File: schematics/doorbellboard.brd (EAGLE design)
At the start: 25.4 x 68.6 mm, 7 parts

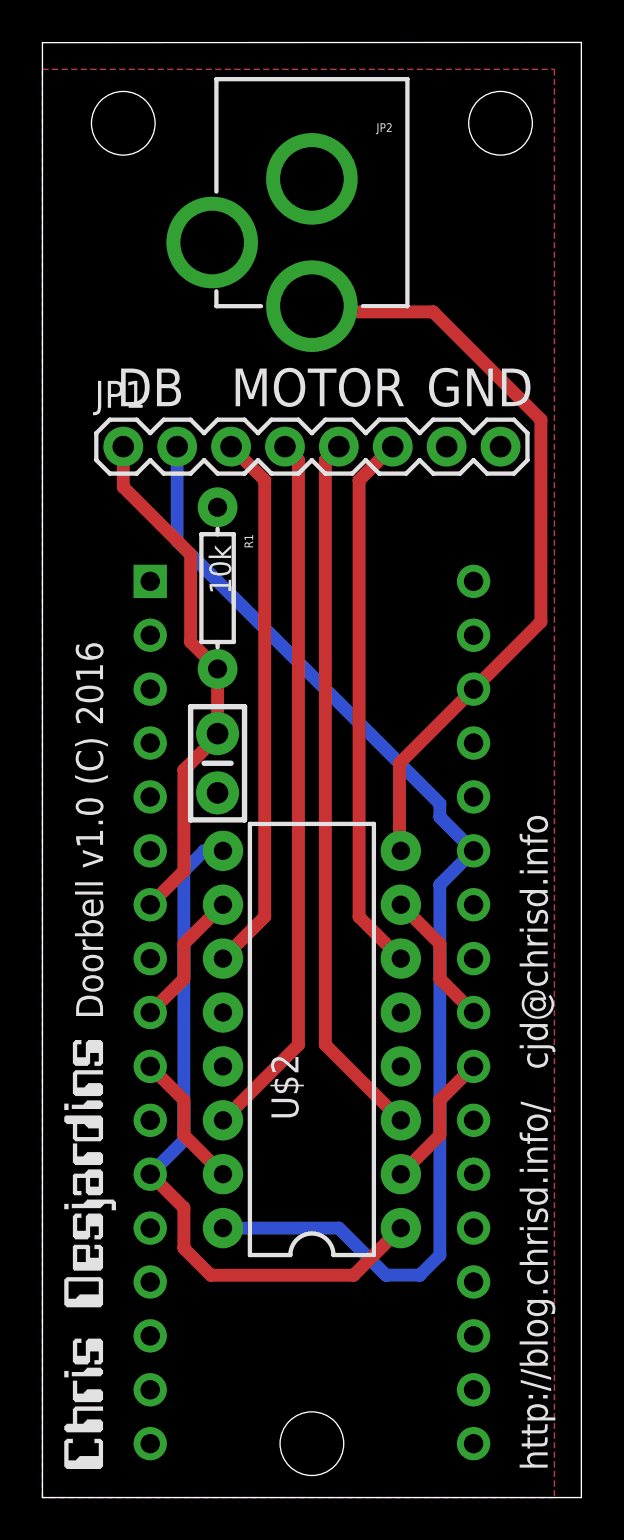
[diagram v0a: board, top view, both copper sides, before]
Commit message: Add OSHW logo
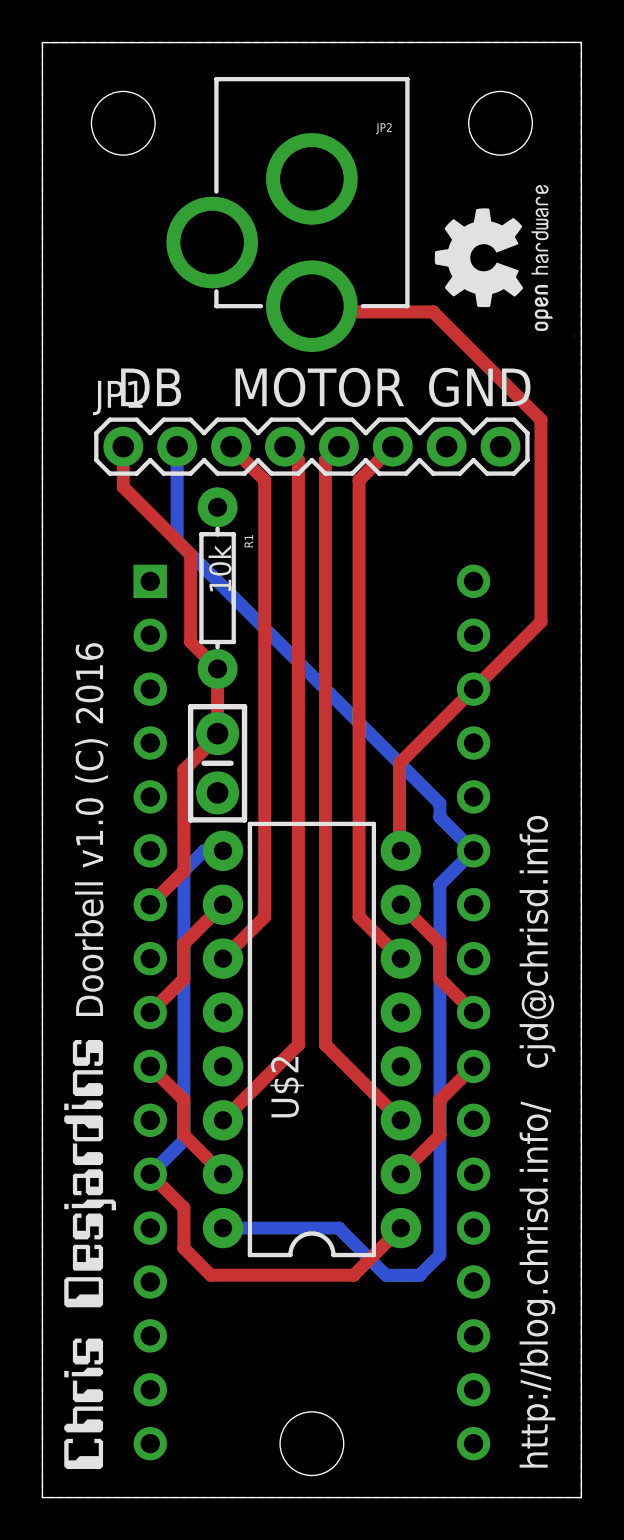
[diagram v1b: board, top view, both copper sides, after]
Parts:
- added U$4: (no value), bfl:OSHW2
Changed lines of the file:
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@@
 </element>
 <element name="U$3" library="desjardins" package="LOGO" value="" x="2.8575" y="1.27" rot="R90"/>
+<element name="U$4" library="bfl" package="OSHW2" value="" x="25.0825" y="54.61" rot="R90"/>
 </elements>
 <signals>
@@
 <polygon width="0.4064" layer="16">
 <vertex x="0" y="0"/>
-<vertex x="0" y="67.31"/>
-<vertex x="24.13" y="67.31"/>
-<vertex x="24.13" y="0"/>
+<vertex x="0" y="68.58"/>
+<vertex x="25.4" y="68.58"/>
+<vertex x="25.4" y="0"/>
 </polygon>
 <polygon width="0.4064" layer="1">
 <vertex x="0" y="0"/>
-<vertex x="0" y="67.31"/>
-<vertex x="24.13" y="67.31"/>
-<vertex x="24.13" y="0"/>
+<vertex x="0" y="68.58"/>
+<vertex x="25.4" y="68.58"/>
+<vertex x="25.4" y="0"/>
 </polygon>
 </signal>

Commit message: Rotate board
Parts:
- moved JP2 80.8 mm to (69.8, 12.7), turned to 90 degrees
- moved U$4 61.8 mm to (54.6, 0.32), turned to 0 degrees
- moved JP1 53.6 mm to (49.5, 21.6), turned to 270 degrees
- moved R1 43.1 mm to (42.9, 17.1), turned to 180 degrees
- moved C1 31.6 mm to (34.6, 17.1), turned to 0 degrees
- moved U$1 23.4 mm to (-1.27, 21.6), turned to 270 degrees
- moved U$3 21.3 mm to (1.27, 22.5), turned to 0 degrees
- moved U$2 12.6 mm to (21.6, 12.7), turned to 0 degrees
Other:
- board size 25.4 x 68.6 mm -> 68.6 x 25.4 mm

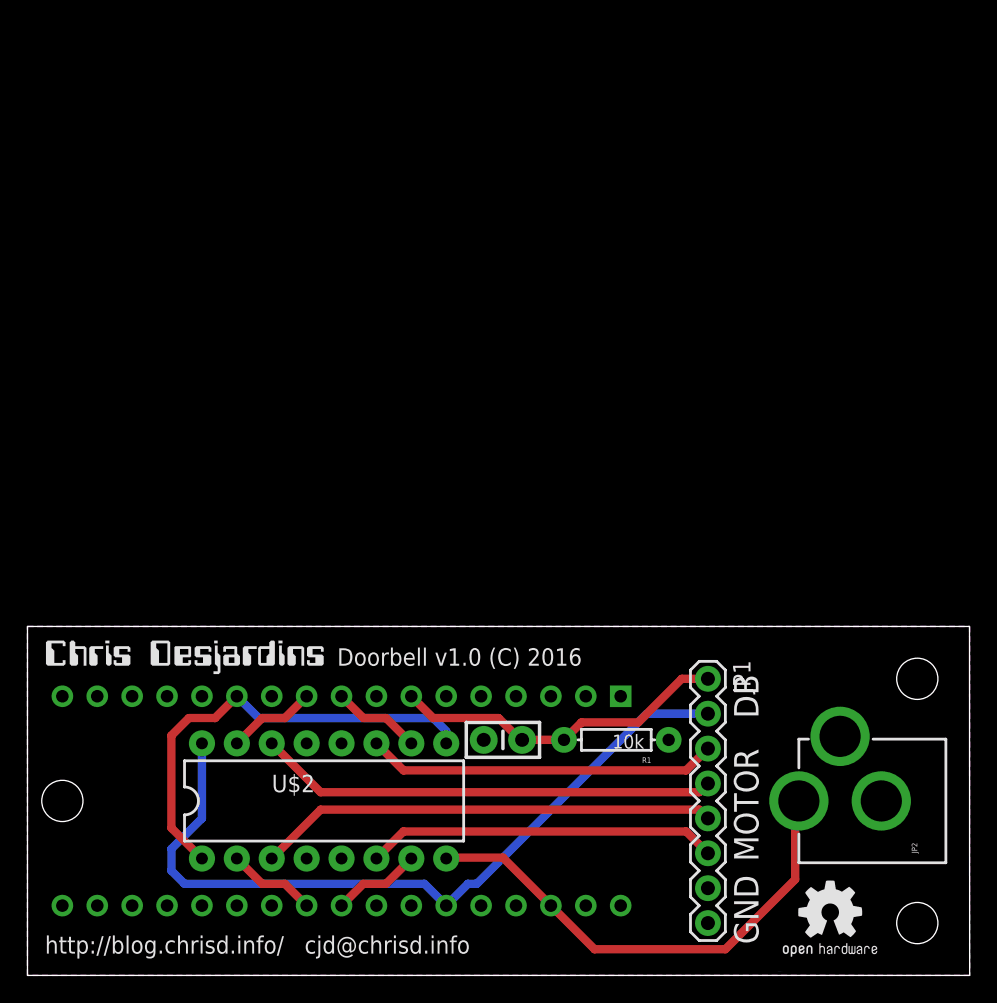
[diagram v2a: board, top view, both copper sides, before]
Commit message: Add some LEDs
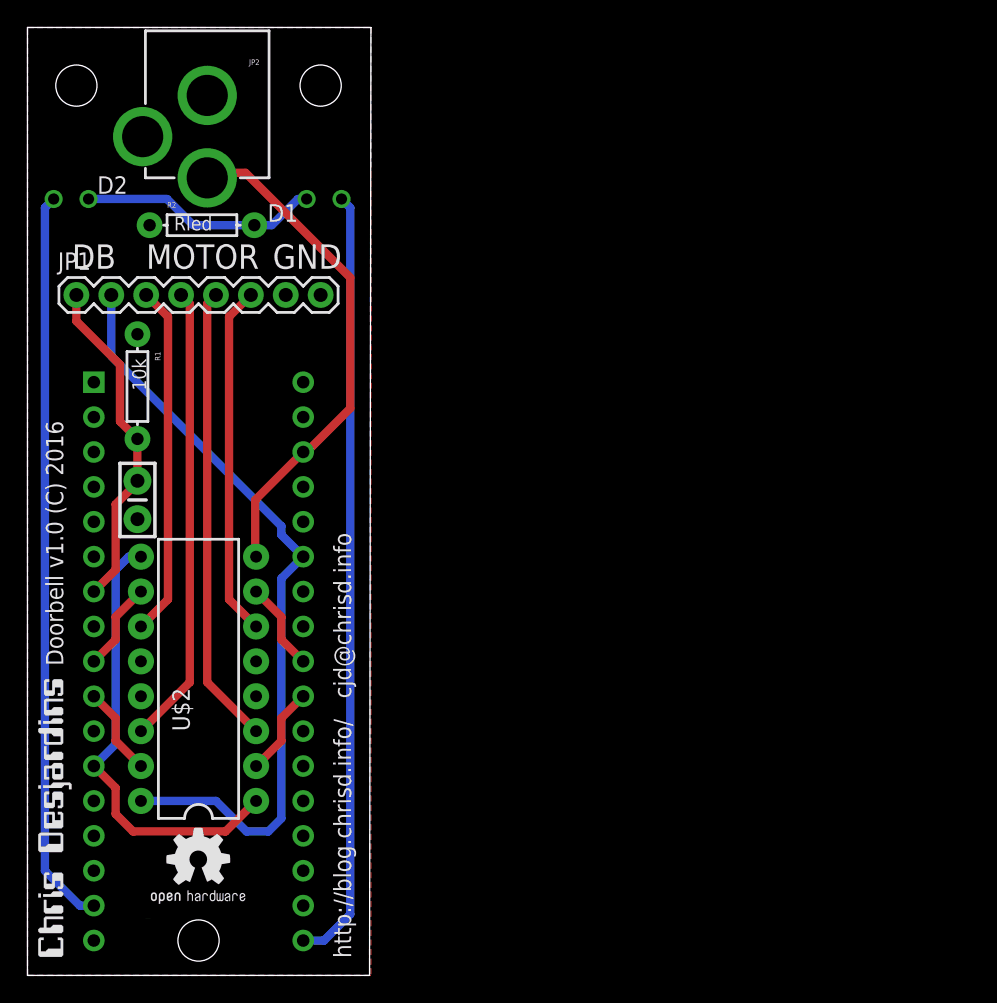
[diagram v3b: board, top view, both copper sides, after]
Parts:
- added D1, D2: (no value), SparkFun-LED:LED3MM-NS
- added R2: Rled, SparkFun-Resistors:AXIAL-0.3
- moved JP2 81.9 mm to (13.1, 71.8), turned to 180 degrees
- moved JP1 53.8 mm to (3.56, 49.5), turned to 0 degrees
- moved U$4 46.2 mm to (8.61, 4.17)
- moved R1 43.3 mm to (8.01, 42.9), turned to 270 degrees
- moved C1 31.8 mm to (8.01, 34.6), turned to 90 degrees
- moved U$1 23.4 mm to (3.56, -1.27), turned to 0 degrees
- moved U$3 21.3 mm to (2.61, 1.27), turned to 90 degrees
- moved U$2 12.8 mm to (12.4, 21.6), turned to 90 degrees
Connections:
- new net LEDA: D1.A, U$1.P18
- new net LEDB: D2.A, U$1.P16
- new net LEDOUT: D1.K, D2.K, R2.P$2
- net GND: now also R2.P$1
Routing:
- net LEDA: track 0.00 -> 56.5 mm
- net LEDB: track 0.00 -> 53.8 mm
- net LEDOUT: track 0.00 -> 17.5 mm
- net VIN: track 36.1 -> 37.1 mm
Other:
- board size 68.6 x 25.4 mm -> 25 x 69 mm
